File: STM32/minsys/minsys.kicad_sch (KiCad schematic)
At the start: 29 parts, among them J1 USB_B_Micro, J2 ST-LINK, J3 BOOT, J4 Conn_01x20, J5 Conn_01x20, SW1 RST, U1 STM32F103C8Tx, U2 AMS1117-3.3, Y1 8MHz, Y2 32.758K

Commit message: edit pcb
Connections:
- net RTCIN is gone; now on net PC14: C6.1, U1.3 (PC14), Y2.1
- net RTCOUT is gone; now on net PC15: C7.1, U1.4 (PC15), Y2.2
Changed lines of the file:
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@@
+		)
+	)
+	(label "PC14"
+		(at 189.23 64.77 0)
+		(effects
+			(font
+				(size 1.27 1.27)
+			)
+			(justify left bottom)
+		)
+	)
+	(label "PC15"
+		(at 189.23 67.31 0)
+		(effects
+			(font
+				(size 1.27 1.27)
+			)
+			(justify left bottom)
 		)
 	)

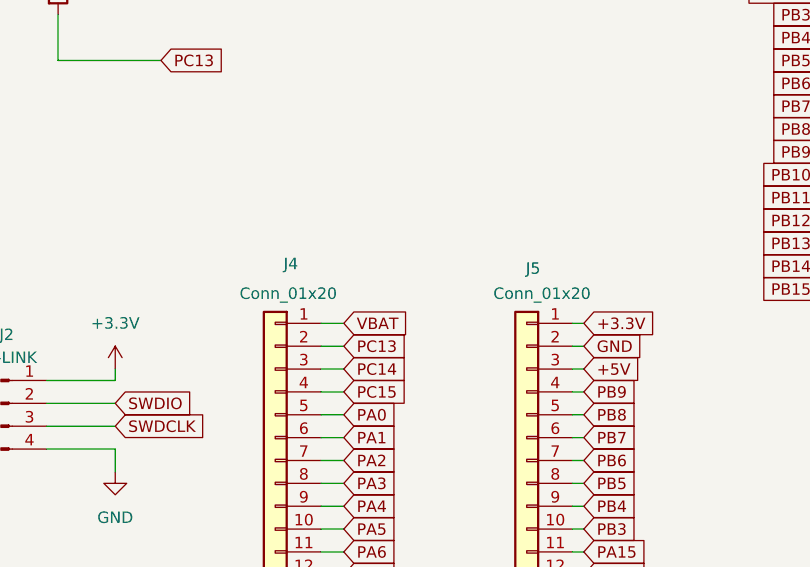
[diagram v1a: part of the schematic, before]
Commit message: add minsys.kicad(copy).pcb
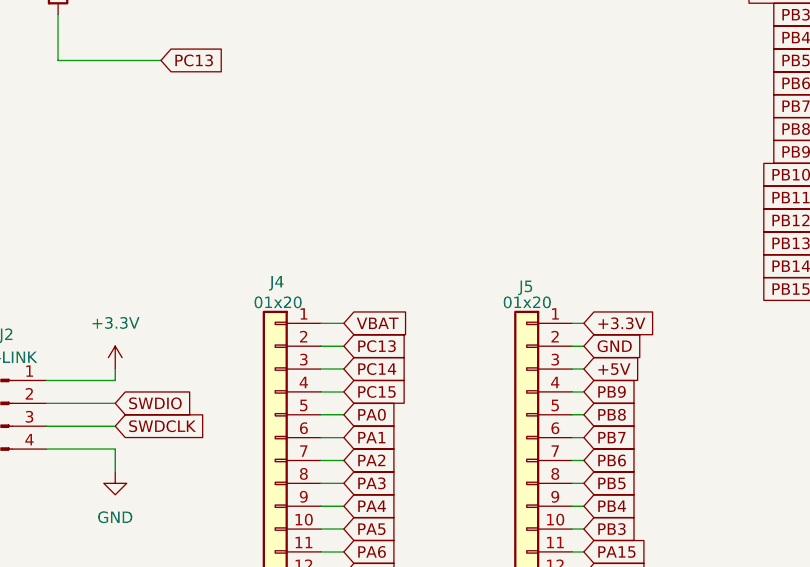
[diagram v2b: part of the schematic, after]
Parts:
- J4, J5: value Conn_01x20 -> 01x20
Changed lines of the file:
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@@
 		(dnp no)
 		(property "Reference" "J4"
-			(at 129.54 107.696 0)
-			(effects
-				(font
-					(size 1.27 1.27)
-				)
-				(justify left)
-			)
-		)
-		(property "Value" "Conn_01x20"
-			(at 133.858 110.998 0)
+			(at 128.016 109.728 0)
+			(effects
+				(font
+					(size 1.27 1.27)
+				)
+				(justify left)
+			)
+		)
+		(property "Value" "01x20"
+			(at 130.048 112.014 0)
 			(effects
 				(font
@@
 		(dnp no)
 		(property "Reference" "J5"
-			(at 156.464 108.204 0)
-			(effects
-				(font
-					(size 1.27 1.27)
-				)
-				(justify left)
-			)
-		)
-		(property "Value" "Conn_01x20"
-			(at 162.052 110.998 0)
-			(effects
-				(font
+			(at 155.702 110.236 0)
+			(effects
+				(font
+					(size 1.27 1.27)
+				)
+				(justify left)
+			)
+		)
+		(property "Value" "01x20"
+			(at 157.734 112.014 0)
+			(effects
+				(font
